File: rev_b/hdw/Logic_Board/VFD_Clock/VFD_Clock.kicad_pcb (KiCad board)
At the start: 4 copper layers, 200 x 50 mm, 486 parts, among them J1501 PICKIT3, J1801 I2C, J1802 USB UART, J1803 BLE UART, J201 +12V IN, J2401 USB_B_Mini, J3001 DSP_IO_Connector, Q1001 IRFL214TRPBF, Q1301 BSS214NW, Q1302 IRLML2060, Q1303 BSS214NW, Q1304 BSS214NW, Q1305 TP0610T, Q1306 IRLML2060, Q1307 BSS214NW, Q1308 IRLML2060, Q1309 BSS214NW, Q1310 TP0610T, Q1501 BSS214NW, Q1801 BSS214NW, Q201 IPC100N04S51R7ATMA1, Q202 IPC100N04S51R7ATMA1, Q2701 BSS214NW, SW1501 MRST, U1001 TLV6700, U1002 LT3757, U1101 MCP9804, U1102 INA219BxDCN, U1103 LTC4151DD, U1201 LTC4419DD, U1202 TPS22929D, U1203 TPS63001, U1401 PIC32MZ2048EFG100_IPT, U1801 LTC6900, U1802 74LVC1G97, U1803 MCP9804, U1901 DS3231MZ, U2001 74LVC1G97, U2002 74LVC1G97, U2003 74LVC1G97, U2004 74LVC1G97, U2005 74LVC1G97, U2006 74LVC1G97, U2007 74LVC1G97, U201 LTC4365DDB, U2101 TPS71533, U2102 74LVC1G97, U2103 74LVC1G97, U2104 74LVC1G97, U2105 74LVC1G97, U2106 74LVC1G97, U2107 74LVC1G97, U2108 74LVC1G97, U2201 TCA9803, U2301 DS1683, U2401 TLV6700, U2402 FT234XD, U2403 TPD3S014DBVR, U2501 ISO7321C, U2502 ISO1541, U2503 TLP185xSE, U2504 74LVC1G97, U2601 INA219BxDCN, U2602 MCP9804, U2701 RN4871, U2801 74VHC541, U2802 74VHC541, U2803 74LVC1G97, U2804 74LVC1G97, U2901 TCA9803, U2902 74VHC541, U301 INA219BxDCN, U302 MCP9804, U401 TPS62130, U501 INA219BxDCN, U502 MCP9804, U503 INA219BxDCN, U601 TPS62130, U701 INA219BxDCN, U702 MCP9804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

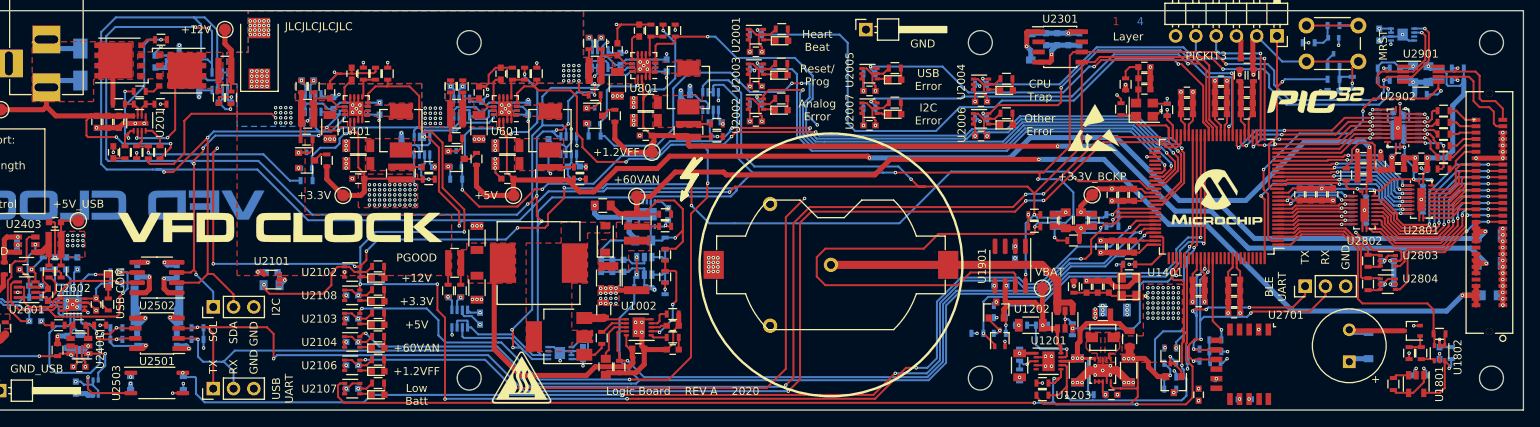
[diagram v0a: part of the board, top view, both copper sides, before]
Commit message: Added USB UART level shifting, few PCB deletions
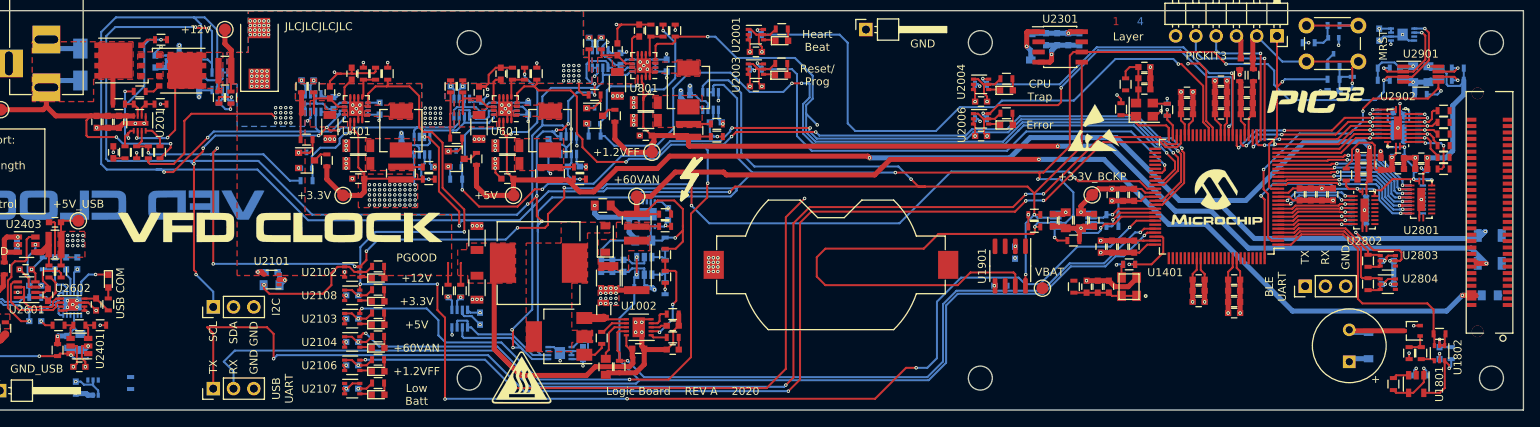
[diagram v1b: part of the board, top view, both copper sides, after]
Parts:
- removed BT1203: TLH-5935/P, Custom Footprints Library:TLH-5935
- removed C1201, C1202, C1203, C1204, C1206, C1207: 10uF, Capacitors_SMD:C_1206
- removed C1205, C2002, C2005, C2007, C2501, C2502, C2504, C2505, C2702: 0.1uF, Capacitors_SMD:C_0603
- removed C1629: 22uF, Capacitors_SMD:C_1206
- removed C2503: 0.56uF, Capacitors_SMD:C_2220
- removed C2701: 10uF, Capacitors_SMD:C_0603
- removed D2002, D2005, D2007: Red, LEDs:LED_0603
- removed L1201: 2.2uH, Inductors_SMD:L_Vishay_IHLP-1212
- removed Q1303, Q1309, Q2701: BSS214NW, TO_SOT_Packages_SMD:SOT-323_SC-70
- removed Q1305, Q1310: TP0610T, Package_TO_SOT_SMD:SOT-23
- removed R1002, R402, R602, R802: 0.02, Resistors_SMD:R_0612
- removed R1201: 84.5k, Resistors_SMD:R_0603
- removed R1202: 45.3k, Resistors_SMD:R_0603
- removed R1203: 1.07M, Resistors_SMD:R_0603
- removed R1204: 196k, Resistors_SMD:R_0603
- removed R1205, R1210: 0, Resistors_SMD:R_0805
- removed R1206, R1208: 562k, Resistors_SMD:R_0603
- removed R1207, R1304, R1305, R1307, R1308, R1311, R1313, R1314, R1315, R2002, R2009, R2013, R2501, R2502, R2503, R2505, R2506, R2507, R2508, R2702, R2703, R2704: 10k, Resistors_SMD:R_0603
- removed R1209: 100, Resistors_SMD:R_0603
- removed R2004, R2011, R2014: 1k, Resistors_SMD:R_0603
- removed R2701: 10, Resistors_SMD:R_0603
- removed U1201: LTC4419DD, Housings_DFN_QFN:DFN-10-1EP_3x3mm_Pitch0.5mm
- removed U1202: TPS22929D, Package_TO_SOT_SMD:SOT-23-6
- removed U1203: TPS63001, Package_SON:Texas_DRC0010J_ThermalVias
- removed U2002, U2005, U2007: 74LVC1G97, Package_TO_SOT_SMD:SOT-363_SC-70-6
- removed U2501: ISO7321C, Housings_SOIC:SOIC-8_3.9x4.9mm_Pitch1.27mm
- removed U2502: ISO1541, Package_SO:SOIC-8_3.9x4.9mm_P1.27mm
- removed U2503: TLP185xSE, Package_SO:SOIC-4_4.55x3.7mm_P2.54mm
- removed U2701: RN4871, RF_Module:Microchip_RN4871
- J3001: value DSP_IO_Connector -> CON60_2X30_USH_ERF8
- moved J3001 11.7 mm to (230.1, 91.5)
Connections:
- J3001 pad 1: GND -> (no net)
- J3001 pad 10: Net-(J3001-Pad10) -> (no net)
- J3001 pad 11: GND -> (no net)
- J3001 pad 12: +1.2VFF -> (no net)
- J3001 pad 13: GND -> (no net)
- J3001 pad 14: +1.2VFF -> (no net)
- J3001 pad 15: GND -> (no net)
- J3001 pad 16: +1.2VFF -> (no net)
- J3001 pad 17: GND -> (no net)
- J3001 pad 18: +1.2VFF -> (no net)
- J3001 pad 19: GND -> (no net)
- J3001 pad 2: +60VAN -> (no net)
- J3001 pad 20: Net-(J3001-Pad20) -> (no net)
- J3001 pad 21: GND -> (no net)
- J3001 pad 22: +5V -> (no net)
- J3001 pad 23: GND -> (no net)
- J3001 pad 24: +5V -> (no net)
- J3001 pad 25: GND -> (no net)
- J3001 pad 26: +5V -> (no net)
- J3001 pad 27: Colon_3_DSP -> (no net)
- J3001 pad 28: +5V -> (no net)
- J3001 pad 29: Colon_2_DSP -> (no net)
- J3001 pad 3: GND -> (no net)
- J3001 pad 30: Net-(J3001-Pad30) -> (no net)
- J3001 pad 31: Colon_1_DSP -> (no net)
- J3001 pad 32: Anode_DP_DSP -> (no net)
- J3001 pad 33: Colon_0_DSP -> (no net)
- J3001 pad 34: Anode_G_DSP -> (no net)
- J3001 pad 35: Grid_5_DSP -> (no net)
- J3001 pad 36: Anode_F_DSP -> (no net)
- J3001 pad 37: Grid_4_DSP -> (no net)
- J3001 pad 38: Anode_E_DSP -> (no net)
- J3001 pad 39: Grid_3_DSP -> (no net)
- J3001 pad 4: +60VAN -> (no net)
- J3001 pad 40: Anode_D_DSP -> (no net)
- J3001 pad 41: Grid_2_DSP -> (no net)
- J3001 pad 42: Anode_C_DSP -> (no net)
- J3001 pad 43: Grid_1_DSP -> (no net)
- J3001 pad 44: Anode_B_DSP -> (no net)
- J3001 pad 45: Grid_0_DSP -> (no net)
- J3001 pad 46: Anode_A_DSP -> (no net)
- J3001 pad 47: GND -> (no net)
- J3001 pad 48: GND -> (no net)
- J3001 pad 49: GND -> (no net)
- J3001 pad 5: GND -> (no net)
- J3001 pad 50: Cap_Touch_Left_DSP -> (no net)
- J3001 pad 51: GND -> (no net)
- J3001 pad 52: Cap_Touch_Right_DSP -> (no net)
- J3001 pad 53: GND -> (no net)
- J3001 pad 54: Cap_Touch_Up_DSP -> (no net)
- J3001 pad 55: GND -> (no net)
- J3001 pad 56: Cap_Touch_Down_DSP -> (no net)
- J3001 pad 57: I2C_DSP_SDA -> (no net)
- J3001 pad 58: Cap_Touch_Power_DSP -> (no net)
- J3001 pad 59: I2C_DSP_SCL -> (no net)
- J3001 pad 6: +60VAN -> (no net)
- J3001 pad 60: ~Display_Detect_DSP -> (no net)
- J3001 pad 7: GND -> (no net)
- J3001 pad 8: +60VAN -> (no net)
- J3001 pad 9: GND -> (no net)
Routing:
- net ~USB_Detect: track 139.9 -> 0.00 mm, vias 4 -> 0
- net VBAT_PGOOD: track 134.6 -> 0.00 mm, vias 3 -> 0
- net Analog_Error_LED: track 66.6 -> 0.00 mm, vias 3 -> 0
- net GND: track 429.4 -> 363.0 mm, vias 233 -> 176
- net USB_Error_LED: track 56.9 -> 0.00 mm, vias 2 -> 0
- net VBAT_ADC_Enable: track 50.4 -> 0.00 mm, vias 2 -> 0
- net I2C_SCL: track 434.0 -> 384.2 mm, vias 23 -> 21
- net I2C_Error_LED: track 55.6 -> 11.1 mm, vias 2 -> 1
- net +3.3V_BCKP: track 125.3 -> 81.1 mm, vias 68 -> 9
- net VBAT_ADC: track 44.2 -> 0.00 mm, vias 1 -> 0
- net BCKP_ON: track 41.8 -> 0.00 mm, vias 2 -> 0
- net BLE_UART_RX: track 36.6 -> 0.00 mm, vias 4 -> 0
- net +3V3: track 221.4 -> 185.1 mm, vias 110 -> 94
- net POS3P3_BCKP_ADC: track 35.9 -> 0.00 mm, vias 1 -> 0
- net Net-(BT1202-Pad1): track 35.8 -> 0.00 mm
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- removed copper zone on F.Cu, net +3.3V_BCKP
- removed copper zone on PWR, net +3.3V_BCKP
- removed copper zone on F.Cu, net Net-(L1201-Pad1)
- removed copper zone on F.Cu, net Net-(L1201-Pad2)
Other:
- board text added: "Error"
- board text removed: "Analog Error"
- board text removed: "I2C Error"
- board text removed: "Other Error"
- board text removed: "USB Error"

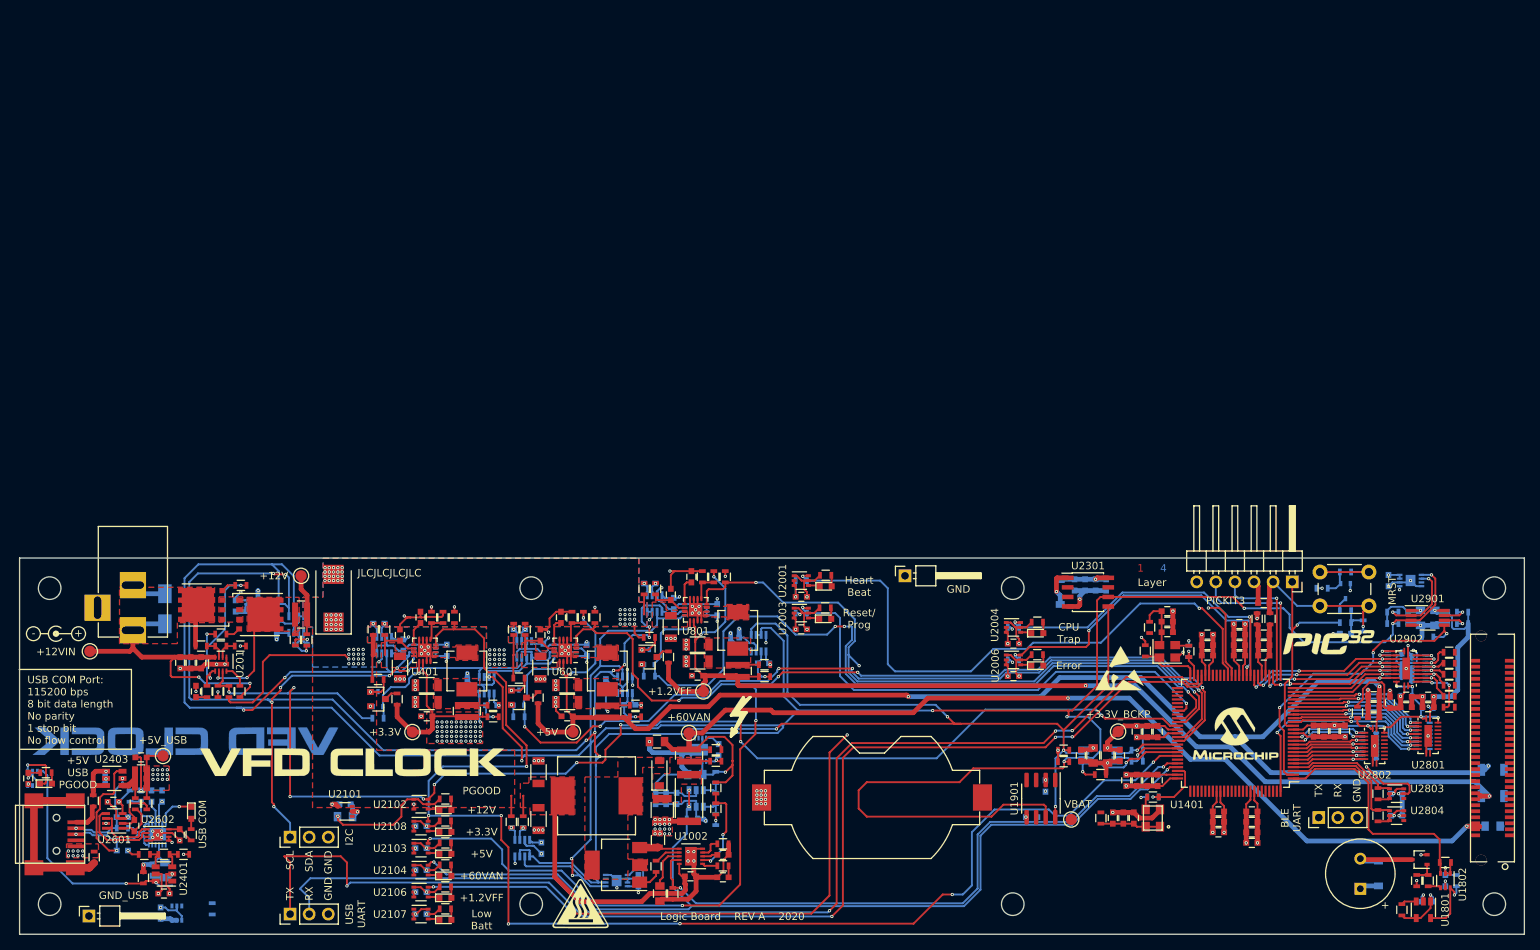
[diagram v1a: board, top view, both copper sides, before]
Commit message: PCB changes, deletions
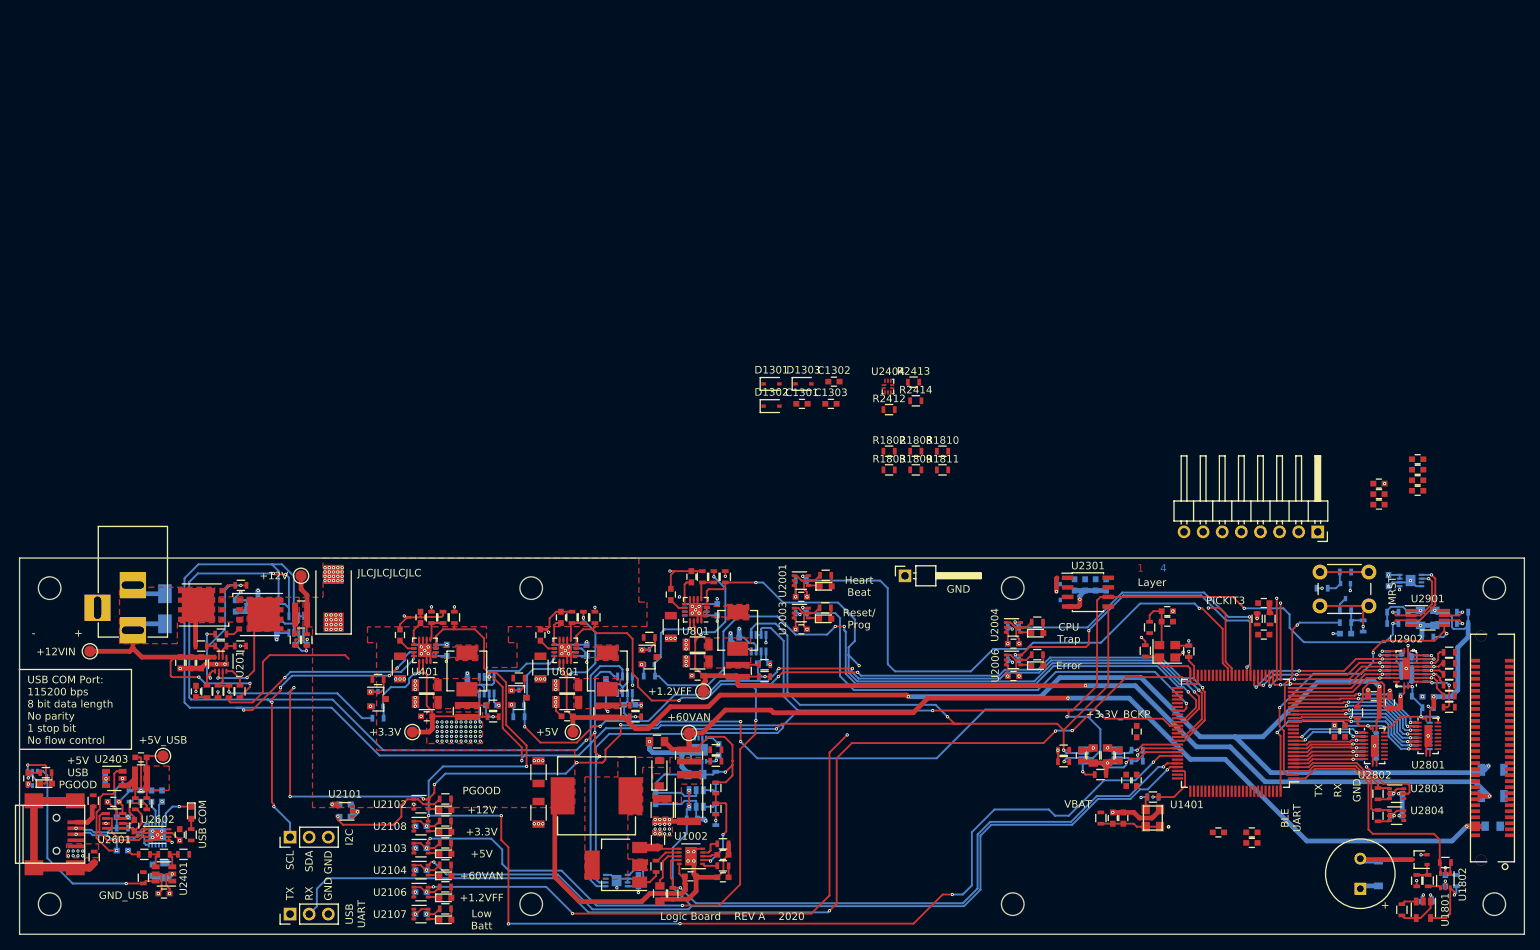
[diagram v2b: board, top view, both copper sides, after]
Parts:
- removed BT1202: CR2032, Battery_Holders:Keystone_1058_1x2032-CoinCell
- removed C1006, C1611, C1612, C1618, C1619, C1625, C1626, C2803, C2804, C2902: 10nF, Capacitors_SMD:C_0603
- removed C1008, C1613, C1614, C1620, C1621, C1627, C1628, C1705, C1706, C2805, C2806, C2903: 1nF, Capacitors_SMD:C_0603
- removed C1101, C1103, C1901, C1902, C2506, C501, C502, C701, C702, C901, C902: 0.1uF, Capacitors_SMD:C_0603
- removed G***: LOGO, Custom Footprints Library:VFD_QR_Code
- removed G***: Heat_Caution_Symbol, Custom Footprints Library:Heat_Caution_Symbol
- removed G***: LOGO, Custom Footprints Library:VFD_Clock_Logo_Mask
- removed G***: LOGO, Custom Footprints Library:VFD_CLock_Logo_Silk
- removed G***: Owl_1_Logo, Custom Footprints Library:Owl_1_Logo
- removed G***: PIC32_Logo, Custom Footprints Library:PIC32_Logo
- removed G***: Microchip_Logo, Custom Footprints Library:Microchip_Logo
- removed J1803: BLE UART, Pin_Headers:Pin_Header_Straight_1x03_Pitch2.54mm
- removed R1001, R1006, R401, R403, R601, R603, R801, R803: 100, Resistors_SMD:R_0603
- removed R1303, R1309, R1312: 237, Resistors_SMD:R_0603
- removed R2504: 1k, Resistors_SMD:R_0603
- removed REF**: Symbol_Barrel_Polarity, Symbol:Symbol_Barrel_Polarity
- removed REF**: KiCAD Logo, Symbols:Symbol_KiCAD-Logo_CopperAndSilkScreenTop
- removed REF**: ESD-Logo_6.6x6mm_SilkScreen, Symbol:ESD-Logo_6.6x6mm_SilkScreen
- removed REF**: Symbol_Highvoltage_Type1_Silk_Small, Custom Footprints Library:Symbol_Highvoltage_Type1_Silk_Small
- removed TP1201, TP1202: TP, Custom Footprints Library:Test_Point
- removed TP2402: TP, Pin_Headers:Pin_Header_Angled_1x01_Pitch2.54mm
- removed U1102, U501, U701, U901: INA219BxDCN, Package_TO_SOT_SMD:SOT-23-8
- removed U1901: DS3231MZ, Package_SO:SOIC-8_3.9x4.9mm_P1.27mm
- removed U2504: 74LVC1G97, Package_TO_SOT_SMD:SOT-363_SC-70-6
- added C1301: 10uF, Capacitors_SMD:C_0603, F.Cu at (138.3, 45.8)
- added C1302: 10uF, Capacitors_SMD:C_0603, F.Cu at (142.6, 42.8)
- added C1303: 10uF, Capacitors_SMD:C_0603, F.Cu at (142.2, 45.8)
- added D1301: BAT48JFILM, Diode_SMD:D_SOD-323, F.Cu at (134.3, 43.1)
- added D1302: BAT48JFILM, Diode_SMD:D_SOD-323, F.Cu at (134.3, 46.1)
- added D1303: BAT48JFILM, Diode_SMD:D_SOD-323, F.Cu at (138.5, 43.1)
- added R1802: 10k, Resistors_SMD:R_0603, F.Cu at (149.9, 52.1)
- added R1803: 10, Resistors_SMD:R_0603, F.Cu at (149.9, 54.6)
- added R1808: 10k, Resistors_SMD:R_0603, F.Cu at (153.5, 52.1)
- added R1809: 10, Resistors_SMD:R_0603, F.Cu at (153.5, 54.6)
- added R1810: 10k, Resistors_SMD:R_0603, F.Cu at (157.0, 52.1)
- added R1811: 10, Resistors_SMD:R_0603, F.Cu at (157.0, 54.6)
- added R2412: 100k, Resistors_SMD:R_0603, F.Cu at (149.9, 46.6)
- added R2413: 100k, Resistors_SMD:R_0603, F.Cu at (153.2, 42.9)
- added R2414: 100k, Resistors_SMD:R_0603, F.Cu at (153.5, 45.4)
- added U2404: SN74AVC2T245, Housings_DFN_QFN:UQFN-10_1.4x1.8mm_Pitch0.4mm, F.Cu at (149.8, 43.5)
- C1604, C1605, C1703, C1704: value 10nF -> 10uF
- C1606, C1607: value 1nF -> 10uF
- C2102: value 4.7uF -> 10uF; footprint Capacitors_SMD:C_0805 -> Capacitors_SMD:C_0603
- D2301: value MBR0530 -> BAT48JFILM; footprint Diode_SMD:D_SOD-123 -> Diode_SMD:D_SOD-323
- J1501: value PICKIT3 -> PICKIT4; footprint Custom Footprints Library:PICKIT3_Header -> Custom Footprints Library:PICKIT4_Header
- J3001: value CON60_2X30_USH_ERF8 -> DSP_IO_Connector
- Q1302, Q1306, Q1308: value IRLML2060 -> ZXMS6004FFTA
- R1014, R1016, R210, R212, R405, R407, R606, R608, R806, R808: value 100 -> 10
- R2401: value 10k -> 100k
- moved C1603 32.3 mm to (220.2, 53.1)
- moved C1604 32.3 mm to (220.2, 55.9)
- moved C1606 32.3 mm to (220.2, 57.3)
- moved C1601 32.3 mm to (220.2, 54.5)
- moved C1605 30.4 mm to (215.0, 57.8)
- moved C1607 30.4 mm to (215.0, 59.2)
- moved C1602 30.4 mm to (215.0, 56.4)
- moved J1501 17.4 mm to (206.9, 62.8)
- moved C1002 0.83 mm to (103.3, 100.1)
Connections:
- net Analog_Error_LED renamed Net-(U1401-Pad58)
- net BCKP_ON renamed Net-(U1401-Pad78)
- net BLE_RESET renamed Net-(U1401-Pad87)
- net I2C_Error_LED renamed Net-(U1401-Pad39)
- net Other_Error_LED renamed Error_LED
- net POS3P3_BCKP_ADC renamed Net-(U1401-Pad44)
- net POS3P3_BCKP_ADC_Enable renamed Net-(U1401-Pad43)
- net USB_Error_LED renamed Net-(U1401-Pad38)
- net VBAT_Enable renamed Net-(U1401-Pad79)
- net ~USB_Detect renamed Net-(U1401-Pad70)
- C1001 pad 1: Net-(C1001-Pad1) -> +12V
- C1002 pad 1: Net-(C1001-Pad1) -> +12V
- C1005 pad 1: Net-(C1001-Pad1) -> +12V
- C1501 pad 1: +3.3V_BCKP -> +3V3
- C1601 pad 1: +3.3V_BCKP -> +3V3
- C1602 pad 1: +3.3V_BCKP -> +3V3
- C1603 pad 1: +3.3V_BCKP -> +3V3
- C1604 pad 1: +3.3V_BCKP -> +3V3
- C1605 pad 1: +3.3V_BCKP -> +3V3
- C1606 pad 1: +3.3V_BCKP -> +3V3
- C1607 pad 1: +3.3V_BCKP -> +3.3VA_MZ
- C1607 pad 2: GND -> GNDA_MZ
- C1608 pad 1: +3.3V_BCKP -> +3V3
- C1609 pad 1: +3.3V_BCKP -> +3V3
- C1610 pad 1: +3.3V_BCKP -> +3V3
- C1615 pad 1: +3.3V_BCKP -> +3V3
- C1616 pad 1: +3.3V_BCKP -> +3V3
- C1617 pad 1: +3.3V_BCKP -> +3V3
- C1622 pad 1: +3.3V_BCKP -> +3V3
- C1623 pad 1: +3.3VA -> +3.3VA_MZ
- C1623 pad 2: GNDA -> GNDA_MZ
- C1624 pad 1: +3.3V_BCKP -> +3V3
- C2105 pad 1: +5V_USB -> +3V3
- C2105 pad 2: GND_USB -> GND
- C2401 pad 1: Net-(C2401-Pad1) -> +3V3
- C2401 pad 2: GND_USB -> GND
- C2402 pad 1: +5V_USB -> +3.3V_USB
- C2402 pad 2: GND_USB -> GND
- C2403 pad 1: +5V_USB -> +3V3
- C2403 pad 2: GND_USB -> GND
- C2404 pad 2: GND_USB -> GND
- C2405 pad 2: GND_USB -> GND
- C2406 pad 2: GND_USB -> GND
- C2407 pad 1: Net-(C2407-Pad1) -> +3.3V_USB
- C2407 pad 2: GND_USB -> GND
- C2408 pad 2: GND_USB -> GND
- C2409 pad 2: GND_USB -> GND
- C2410 pad 1: Net-(C2410-Pad1) -> +3.3V_USB
- C2410 pad 2: GND_USB -> GND
- C2602 pad 1: +5V_USB -> +3V3
- C2602 pad 2: GND_USB -> GND
- C2603 pad 1: +5V_USB -> +3V3
- C2603 pad 2: GND_USB -> GND
- C401 pad 1: Net-(C401-Pad1) -> +12V
- C403 pad 1: Net-(C401-Pad1) -> +12V
- C601 pad 1: Net-(C601-Pad1) -> +12V
- C603 pad 1: Net-(C601-Pad1) -> +12V
- C801 pad 1: Net-(C801-Pad1) -> +12V
- C803 pad 1: Net-(C801-Pad1) -> +12V
- J1501 pad 2: +3.3V_BCKP -> +3V3
- J2401 pad 5: GND_USB -> GND
- J3001 pad 1: (no net) -> GND
- J3001 pad 10: (no net) -> Net-(J3001-Pad10)
- J3001 pad 11: (no net) -> GND
- J3001 pad 12: (no net) -> +1.2VFF
- J3001 pad 13: (no net) -> GND
- J3001 pad 14: (no net) -> +1.2VFF
- J3001 pad 15: (no net) -> GND
- J3001 pad 16: (no net) -> +1.2VFF
- J3001 pad 17: (no net) -> GND
- J3001 pad 18: (no net) -> +1.2VFF
- J3001 pad 19: (no net) -> GND
- J3001 pad 2: (no net) -> +60VAN
- J3001 pad 20: (no net) -> Net-(J3001-Pad20)
- J3001 pad 21: (no net) -> GND
- J3001 pad 22: (no net) -> +5V
- J3001 pad 23: (no net) -> GND
- J3001 pad 24: (no net) -> +5V
- J3001 pad 25: (no net) -> GND
- J3001 pad 26: (no net) -> +5V
- J3001 pad 27: (no net) -> Colon_3_DSP
- J3001 pad 28: (no net) -> +5V
- J3001 pad 29: (no net) -> Colon_2_DSP
- J3001 pad 3: (no net) -> GND
- J3001 pad 30: (no net) -> Net-(J3001-Pad30)
- J3001 pad 31: (no net) -> Colon_1_DSP
- J3001 pad 32: (no net) -> Anode_DP_DSP
- J3001 pad 33: (no net) -> Colon_0_DSP
- J3001 pad 34: (no net) -> Anode_G_DSP
- J3001 pad 35: (no net) -> Grid_5_DSP
- J3001 pad 36: (no net) -> Anode_F_DSP
- J3001 pad 37: (no net) -> Grid_4_DSP
- J3001 pad 38: (no net) -> Anode_E_DSP
- J3001 pad 39: (no net) -> Grid_3_DSP
- J3001 pad 4: (no net) -> +60VAN
- J3001 pad 40: (no net) -> Anode_D_DSP
- J3001 pad 41: (no net) -> Grid_2_DSP
- J3001 pad 42: (no net) -> Anode_C_DSP
- J3001 pad 43: (no net) -> Grid_1_DSP
- J3001 pad 44: (no net) -> Anode_B_DSP
- J3001 pad 45: (no net) -> Grid_0_DSP
- J3001 pad 46: (no net) -> Anode_A_DSP
- J3001 pad 47: (no net) -> GND
- J3001 pad 48: (no net) -> GND
- J3001 pad 49: (no net) -> GND
- J3001 pad 5: (no net) -> GND
- J3001 pad 50: (no net) -> Cap_Touch_Left_DSP
- J3001 pad 51: (no net) -> GND
- J3001 pad 52: (no net) -> Cap_Touch_Right_DSP
- J3001 pad 53: (no net) -> GND
- J3001 pad 54: (no net) -> Cap_Touch_Up_DSP
- J3001 pad 55: (no net) -> GND
- J3001 pad 56: (no net) -> Cap_Touch_Down_DSP
- J3001 pad 57: (no net) -> I2C_DSP_SDA
- J3001 pad 58: (no net) -> Cap_Touch_Power_DSP
- J3001 pad 59: (no net) -> I2C_DSP_SCL
- J3001 pad 6: (no net) -> +60VAN
- J3001 pad 60: (no net) -> ~Display_Detect_DSP
- J3001 pad 7: (no net) -> GND
- J3001 pad 8: (no net) -> +60VAN
- J3001 pad 9: (no net) -> GND
- L1001 pad 1: Net-(C1001-Pad1) -> +12V
- L1601 pad 1: +3.3VA -> +3.3VA_MZ
- L1601 pad 2: +3.3V_BCKP -> +3V3
- L1602 pad 1: GNDA -> GNDA_MZ
- L2401 pad 2: Net-(C2410-Pad1) -> Net-(L2401-Pad2)
- L2402 pad 1: GND_USB -> GND
- Q1302 pad 3: Net-(Q1302-Pad3) -> +3V3
- Q1306 pad 3: Net-(Q1306-Pad3) -> +5V
- Q1308 pad 3: Net-(Q1308-Pad3) -> +1.2VFF
- R1014 pad 1: POS60_VAN_SNS_OUT+ -> Net-(C1010-Pad1)
- R1014 pad 2: Net-(C1010-Pad1) -> POS60_VAN_SNS_OUT+
- R1016 pad 1: POS60_VAN_SNS_OUT- -> +60VAN
- R1016 pad 2: +60VAN -> POS60_VAN_SNS_OUT-
- R1302 pad 2: +12V -> Net-(C1301-Pad1)
- R1306 pad 2: +12V -> Net-(C1302-Pad1)
- R1310 pad 2: +12V -> Net-(C1303-Pad1)
- R1504 pad 1: +3.3V_BCKP -> +3V3
- R2104 pad 1: +5V_USB -> +3V3
- R2401 pad 1: +5V_USB -> +3V3
- R2401 pad 2: Net-(C2401-Pad1) -> USB_UART_TX
- R2404 pad 2: GND_USB -> GND
- R2405 pad 1: +5V_USB -> +3V3
- SW1501 pad 1: +3.3V_BCKP -> +3V3
- U1002 pad 10: Net-(C1001-Pad1) -> +12V
- U1401 pad 14: +3.3V_BCKP -> +3V3
- U1401 pad 37: +3.3V_BCKP -> +3V3
- U1401 pad 46: +3.3V_BCKP -> +3V3
- U1401 pad 62: +3.3V_BCKP -> +3V3
- U1401 pad 74: +3.3V_BCKP -> +3V3
- U1401 pad 83: +3.3V_BCKP -> +3V3
- U1401 pad 85: BLE_UART_TX -> Net-(U1401-Pad85)
- U1401 pad 86: BLE_UART_RX -> Net-(U1401-Pad86)
- U1401 pad 93: +3.3V_BCKP -> +3V3
- U2105 pad 1: +5V_USB -> +3V3
- U2105 pad 2: GND_USB -> GND
- U2105 pad 3: GND_USB -> GND
- U2105 pad 5: +5V_USB -> +3V3
- U2401 pad 2: GND_USB -> GND
- U2401 pad 5: +5V_USB -> +3V3
- U2402 pad 10: USB_UART_TX_ISO -> USB_UART_TX_BUF
- U2402 pad 13: GND_USB -> GND
- U2402 pad 2: Net-(C2401-Pad1) -> Net-(U2402-Pad2)
- U2402 pad 3: Net-(C2407-Pad1) -> +3.3V_USB
- U2402 pad 5: GND_USB -> GND
- U2402 pad 7: USB_UART_RX_ISO -> USB_UART_RX_BUF
- U2402 pad 9: +5V_USB -> +3.3V_USB
- U2403 pad 1: Net-(C2410-Pad1) -> Net-(L2401-Pad2)
- U2403 pad 2: GND_USB -> GND
- U2403 pad 3: Net-(C2410-Pad1) -> Net-(L2401-Pad2)
- U2601 pad 3: GND_USB -> GND
- U2601 pad 4: +5V_USB -> +3V3
- U2601 pad 5: I2C_USB_SCL -> I2C_SCL
- U2601 pad 6: I2C_USB_SDA -> I2C_SDA
- U2601 pad 7: GND_USB -> GND
- U2601 pad 8: I2C_USB_SDA -> I2C_SDA
- U2602 pad 1: I2C_USB_SDA -> I2C_SDA
- U2602 pad 2: I2C_USB_SCL -> I2C_SCL
- U2602 pad 4: GND_USB -> GND
- U2602 pad 5: +5V_USB -> +3V3
- U2602 pad 6: +5V_USB -> +3V3
- U2602 pad 7: GND_USB -> GND
- U2602 pad 8: +5V_USB -> +3V3
- U2602 pad 9: GND_USB -> GND
- U401 pad 10: Net-(C401-Pad1) -> +12V
- U401 pad 11: Net-(C401-Pad1) -> +12V
- U401 pad 12: Net-(C401-Pad1) -> +12V
- U601 pad 10: Net-(C601-Pad1) -> +12V
- U601 pad 11: Net-(C601-Pad1) -> +12V
- U601 pad 12: Net-(C601-Pad1) -> +12V
- U801 pad 10: Net-(C801-Pad1) -> +12V
- U801 pad 11: Net-(C801-Pad1) -> +12V
- U801 pad 12: Net-(C801-Pad1) -> +12V
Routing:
- net USB_UART_TX: track 161.3 -> 0.00 mm, vias 4 -> 0
- net I2C_SDA: track 465.0 -> 381.4 mm, vias 12 -> 10
- net +3.3V_BCKP: track 81.1 -> 4.47 mm, vias 9 -> 1
- net I2C_SCL: track 384.2 -> 323.2 mm, vias 21 -> 15
- net GND: track 363.0 -> 307.4 mm, vias 176 -> 177
- net Net-(C1001-Pad1): track 37.4 -> 0.00 mm
- net GND_USB: track 30.5 -> 0.00 mm, vias 24 -> 0
- net +5V_USB: track 40.6 -> 10.8 mm, vias 20 -> 1
- net +12V: track 51.5 -> 73.6 mm, vias 65 -> 17
- net I2C_USB_SCL: track 11.0 -> 0.00 mm
- net ICSPCLK: track 20.6 -> 9.61 mm
- net I2C_USB_SDA: track 9.15 -> 0.00 mm
- net Net-(C601-Pad1): track 8.82 -> 0.00 mm
- net Net-(C2301-Pad1): track 7.88 -> 0.00 mm, vias 1 -> 0
- net +5V: track 242.7 -> 234.9 mm
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- removed copper zone on B.Cu, net +12V
- removed copper zone on PWR, net +5V_USB
- removed copper zone on F.Cu, net GND_USB
- removed copper zone on GND, net GND_USB
- removed copper zone on F.Cu, net Net-(C1001-Pad1)
- removed copper zone on F.Cu, net Net-(C401-Pad1)
- removed copper zone on F.Cu, net Net-(C601-Pad1)
- removed copper zone on F.Cu, net Net-(C801-Pad1)
